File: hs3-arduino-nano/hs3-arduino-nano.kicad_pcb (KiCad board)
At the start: 2 copper layers, 17.8 x 43.2 mm, 41 parts, among them J1 USB_C_Receptacle_USB2.0, J3 DBG, J4 LED, J6 CONN_01x04, P3 CONN_01X01, P4 CONN_01X01, P5 CONN_01X01, P6 CONN_01X01, SW1 Boot, U1 W25Q128JVS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

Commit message: Adding manufacturing files
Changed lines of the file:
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@@
   )
   (layers
-    (0 "F.Cu" signal "Górna sygnałowa")
-    (31 "B.Cu" signal "Dolna sygnałowa")
+    (0 "F.Cu" signal)
+    (31 "B.Cu" signal)
     (32 "B.Adhes" user "B.Adhesive")
     (33 "F.Adhes" user "F.Adhesive")
-    (34 "B.Paste" user "Dolna pasty")
-    (35 "F.Paste" user "Górna pasty")
+    (34 "B.Paste" user)
+    (35 "F.Paste" user)
     (36 "B.SilkS" user "B.Silkscreen")
     (37 "F.SilkS" user "F.Silkscreen")
-    (38 "B.Mask" user "Dolna sodermaski")
-    (39 "F.Mask" user "Górna soldermaski")
+    (38 "B.Mask" user)
+    (39 "F.Mask" user)
     (40 "Dwgs.User" user "User.Drawings")
     (41 "Cmts.User" user "User.Comments")
     (42 "Eco1.User" user "User.Eco1")
     (43 "Eco2.User" user "User.Eco2")
-    (44 "Edge.Cuts" user "Krawędziowa")
+    (44 "Edge.Cuts" user)
     (45 "Margin" user "Marginesu")
     (46 "B.CrtYd" user "B.Courtyard")
     (47 "F.CrtYd" user "F.Courtyard")
-    (48 "B.Fab" user "Dolna produkcyjna")
-    (49 "F.Fab" user "Górna produkcyjna")
+    (48 "B.Fab" user "B.Manufacturing")
+    (49 "F.Fab" user "F.Manufacturing")
   )
   (setup
@@
     (aux_axis_origin 138.176 110.617)
     (pcbplotparams
-      (layerselection 0x0000030_80000001)
+      (layerselection 0x00010fc_ffffffff)
       (disableapertmacros false)
-      (usegerberextensions false)
-      (usegerberattributes true)
-      (usegerberadvancedattributes true)
-      (creategerberjobfile true)
+      (usegerberextensions true)
+      (usegerberattributes false)
+      (usegerberadvancedattributes false)
+      (creategerberjobfile false)
       (svguseinch false)
       (svgprecision 6)
@@
       (psa4output false)
       (plotreference true)
-      (plotvalue true)
+      (plotvalue false)
       (plotinvisibletext false)
       (sketchpadsonfab false)
-      (subtractmaskfromsilk false)
+      (subtractmaskfromsilk true)
       (outputformat 1)
       (mirror false)
-      (drillshape 1)
+      (drillshape 0)
       (scaleselection 1)
-      (outputdirectory "")
+      (outputdirectory "manufacturing/")
     )
   )
@@
     (pad "4" smd roundrect (at 1.5 1.325 180) (size 0.6 1.55) (layers "F.Cu" "F.Paste" "F.Mask") (roundrect_rratio 0.25)
       (net 1 "GND") (pinfunction "Pin_4") (pintype "passive"))
-    (pad "MP" smd roundrect (at 2.8 -1.2 180) (size 1.2 1.8) (layers "F.Cu" "F.Paste" "F.Mask") (roundrect_rratio 0.208333))
-    (pad "MP" smd roundrect (at -2.8 -1.2 180) (size 1.2 1.8) (layers "F.Cu" "F.Paste" "F.Mask") (roundrect_rratio 0.208333))
+    (pad "MP" smd roundrect (at 2.8 -1.2 180) (size 1.2 1.8) (layers "F.Cu" "F.Paste" "F.Mask") (roundrect_rratio 0.2083333333))
+    (pad "MP" smd roundrect (at -2.8 -1.2 180) (size 1.2 1.8) (layers "F.Cu" "F.Paste" "F.Mask") (roundrect_rratio 0.2083333333))
     (model "${KICAD6_3DMODEL_DIR}/Connector_JST.3dshapes/JST_SH_BM04B-SRSS-TB_1x04-1MP_P1.00mm_Vertical.wrl"
       (offset (xyz 0 0 0))
@@
     (pad "4" smd roundrect (at 1.5 1.325) (size 0.6 1.55) (layers "F.Cu" "F.Paste" "F.Mask") (roundrect_rratio 0.25)
       (net 1 "GND") (pinfunction "Pin_4") (pintype "passive"))
-    (pad "MP" smd roundrect (at 2.8 -1.2) (size 1.2 1.8) (layers "F.Cu" "F.Paste" "F.Mask") (roundrect_rratio 0.208333))
-    (pad "MP" smd roundrect (at -2.8 -1.2) (size 1.2 1.8) (layers "F.Cu" "F.Paste" "F.Mask") (roundrect_rratio 0.208333))
+    (pad "MP" smd roundrect (at 2.8 -1.2) (size 1.2 1.8) (layers "F.Cu" "F.Paste" "F.Mask") (roundrect_rratio 0.2083333333))
+    (pad "MP" smd roundrect (at -2.8 -1.2) (size 1.2 1.8) (layers "F.Cu" "F.Paste" "F.Mask") (roundrect_rratio 0.2083333333))
     (model "${KICAD6_3DMODEL_DIR}/Connector_JST.3dshapes/JST_SH_BM04B-SRSS-TB_1x04-1MP_P1.00mm_Vertical.wrl" hide
       (offset (xyz 0 0 0))
@@
     (pad "4" smd roundrect (at 1.5 1.325 180) (size 0.6 1.55) (layers "F.Cu" "F.Paste" "F.Mask") (roundrect_rratio 0.25)
       (net 1 "GND") (pinfunction "Pin_4") (pintype "passive"))
-    (pad "MP" smd roundrect (at -2.8 -1.2 180) (size 1.2 1.8) (layers "F.Cu" "F.Paste" "F.Mask") (roundrect_rratio 0.208333))
-    (pad "MP" smd roundrect (at 2.8 -1.2 180) (size 1.2 1.8) (layers "F.Cu" "F.Paste" "F.Mask") (roundrect_rratio 0.208333))
+    (pad "MP" smd roundrect (at -2.8 -1.2 180) (size 1.2 1.8) (layers "F.Cu" "F.Paste" "F.Mask") (roundrect_rratio 0.2083333333))
+    (pad "MP" smd roundrect (at 2.8 -1.2 180) (size 1.2 1.8) (layers "F.Cu" "F.Paste" "F.Mask") (roundrect_rratio 0.2083333333))
     (model "${KICAD6_3DMODEL_DIR}/Connector_JST.3dshapes/JST_SH_BM04B-SRSS-TB_1x04-1MP_P1.00mm_Vertical.wrl"
       (offset (xyz 0 0 0))
@@
     (pad "4" smd roundrect (at 1.5 1.325) (size 0.6 1.55) (layers "F.Cu" "F.Paste" "F.Mask") (roundrect_rratio 0.25)
       (net 1 "GND") (pinfunction "Pin_4") (pintype "passive"))
-    (pad "MP" smd roundrect (at 2.8 -1.2) (size 1.2 1.8) (layers "F.Cu" "F.Paste" "F.Mask") (roundrect_rratio 0.208333))
-    (pad "MP" smd roundrect (at -2.8 -1.2) (size 1.2 1.8) (layers "F.Cu" "F.Paste" "F.Mask") (roundrect_rratio 0.208333))
+    (pad "MP" smd roundrect (at 2.8 -1.2) (size 1.2 1.8) (layers "F.Cu" "F.Paste" "F.Mask") (roundrect_rratio 0.2083333333))
+    (pad "MP" smd roundrect (at -2.8 -1.2) (size 1.2 1.8) (layers "F.Cu" "F.Paste" "F.Mask") (roundrect_rratio 0.2083333333))
     (model "${KICAD6_3DMODEL_DIR}/Connector_JST.3dshapes/JST_SH_BM04B-SRSS-TB_1x04-1MP_P1.00mm_Vertical.wrl"
       (offset (xyz 0 0 0))
@@
     (fp_line (start 3.5 3.5) (end -3.5 3.5) (layer "F.Fab") (width 0.1))
     (fp_line (start -3.5 -2.5) (end -2.5 -3.5) (layer "F.Fab") (width 0.1))
-    (pad "" smd roundrect (at -0.6375 -0.6375 180) (size 1.084435 1.084435) (layers "F.Paste") (roundrect_rratio 0.230535))
-    (pad "" smd roundrect (at -0.6375 0.6375 180) (size 1.084435 1.084435) (layers "F.Paste") (roundrect_rratio 0.230535))
-    (pad "" smd roundrect (at 0.6375 -0.6375 180) (size 1.084435 1.084435) (layers "F.Paste") (roundrect_rratio 0.230535))
-    (pad "" smd roundrect (at 0.6375 0.6375 180) (size 1.084435 1.084435) (layers "F.Paste") (roundrect_rratio 0.230535))
+    (pad "" smd roundrect (at -0.6375 -0.6375 180) (size 1.084435 1.084435) (layers "F.Paste") (roundrect_rratio 0.2305347946))
+    (pad "" smd roundrect (at -0.6375 0.6375 180) (size 1.084435 1.084435) (layers "F.Paste") (roundrect_rratio 0.2305347946))
+    (pad "" smd roundrect (at 0.6375 -0.6375 180) (size 1.084435 1.084435) (layers "F.Paste") (roundrect_rratio 0.2305347946))
+    (pad "" smd roundrect (at 0.6375 0.6375 180) (size 1.084435 1.084435) (layers "F.Paste") (roundrect_rratio 0.2305347946))
     (pad "1" smd roundrect (at -3.4375 -2.6 180) (size 0.875 0.2) (layers "F.Cu" "F.Paste" "F.Mask") (roundrect_rratio 0.25)
       (net 5 "+3V3") (pinfunction "IOVDD") (pintype "power_in"))

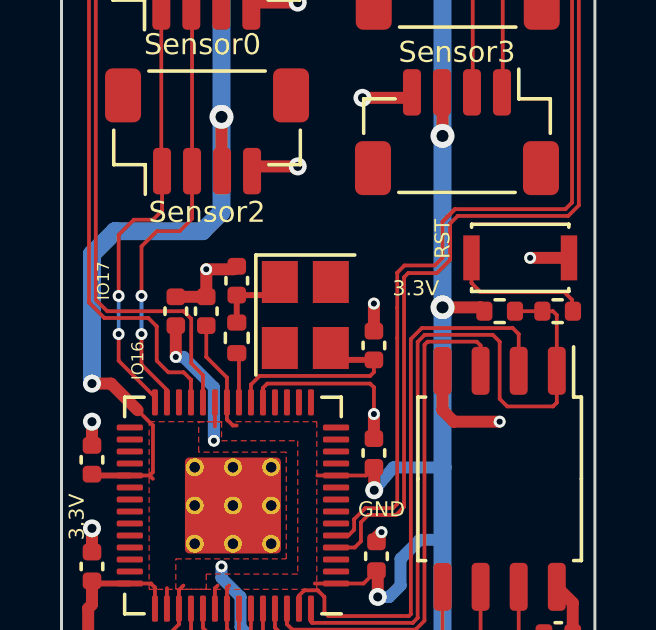
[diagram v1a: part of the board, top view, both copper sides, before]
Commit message: Fixing footprint for xtal
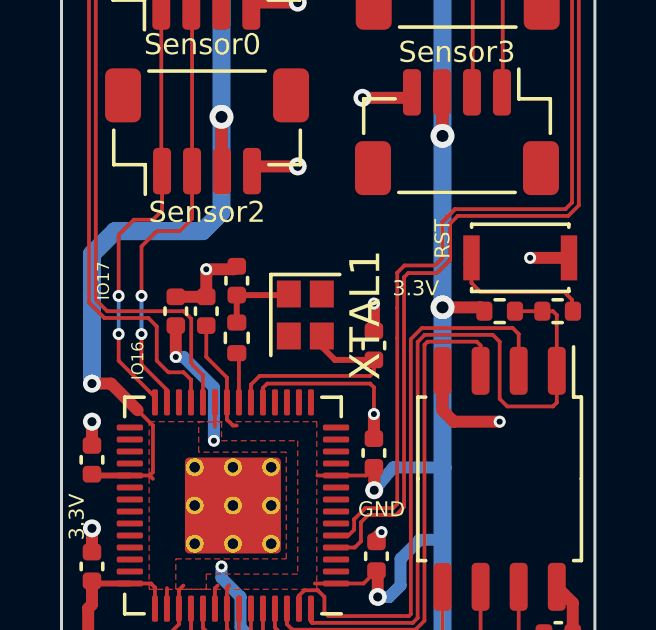
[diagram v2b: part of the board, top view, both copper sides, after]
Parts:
- XTAL1: footprint Crystal:Crystal_SMD_3225-4Pin_3.2x2.5mm -> Crystal:Crystal_SMD_2016-4Pin_2.0x1.6mm
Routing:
- net /XIN: track 6.87 -> 7.55 mm

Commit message: Fixing incorrect XTAL1 part number
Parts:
- R5: value 1k -> 0
- XTAL1: value XRCGB27M120F3M00R0 -> OT201612MJBA4SL
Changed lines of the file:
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@@
     (tags "resistor")
     (property "JLC" "0402")
-    (property "LCSC" "C25905")
+    (property "LCSC" "C17168")
     (property "Sheetfile" "hs3-arduino-nano.kicad_sch")
     (property "Sheetname" "")
@@
       (effects (font (size 1 1) (thickness 0.15)))
     )
-    (fp_text value "1k" (at 0 1.17 90) (layer "F.Fab")
+    (fp_text value "0" (at 0 1.17 90) (layer "F.Fab")
       (effects (font (size 1 1) (thickness 0.15)))
     )
@@
     (descr "SMD Crystal SERIES SMD2016/4 http://www.q-crystal.com/upload/5/2015552223166229.pdf, 2.0x1.6mm^2 package")
     (tags "SMD SMT crystal")
-    (property "JLC" "SMD2016")
-    (property "LCSC" "C576558")
+    (property "JLC" "SMD-2016-4P")
+    (property "LCSC" "C669076")
     (property "Sheetfile" "hs3-arduino-nano.kicad_sch")
     (property "Sheetname" "")
@@
       (effects (font (size 1 1) (thickness 0.15)))
     )
-    (fp_text value "XRCGB27M120F3M00R0" (at 0 2 -90) (layer "F.Fab")
-      (effects (font (size 1 1) (thickness 0.15)))
-    )
+    (fp_text value "OT201612MJBA4SL" (at 0 2 -90) (layer "F.Fab")
+      (effects (font (size 1 1) (thickness 0.15)))
+    )
